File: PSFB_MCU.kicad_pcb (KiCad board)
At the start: 4 copper layers, 238 parts, among them J2 Power_IN, Q1 WMM043N10HGD, Q2 WMM043N10HGD, Q3 WMM043N10HGD, Q4 WMM043N10HGD, U10 USBLC6-2SC6, U11 USBLC6-2SC6, U12 USBLC6-2SC6, U13 USBLC6-2SC6, U14 USBLC6-2SC6, U4 AMS1117-5.0, U5 AMS1117-3.3, U6 LM5176PWP, U7 USBLC6-2SC6, U8 USBLC6-2SC6, U9 USBLC6-2SC6, Y1 16M

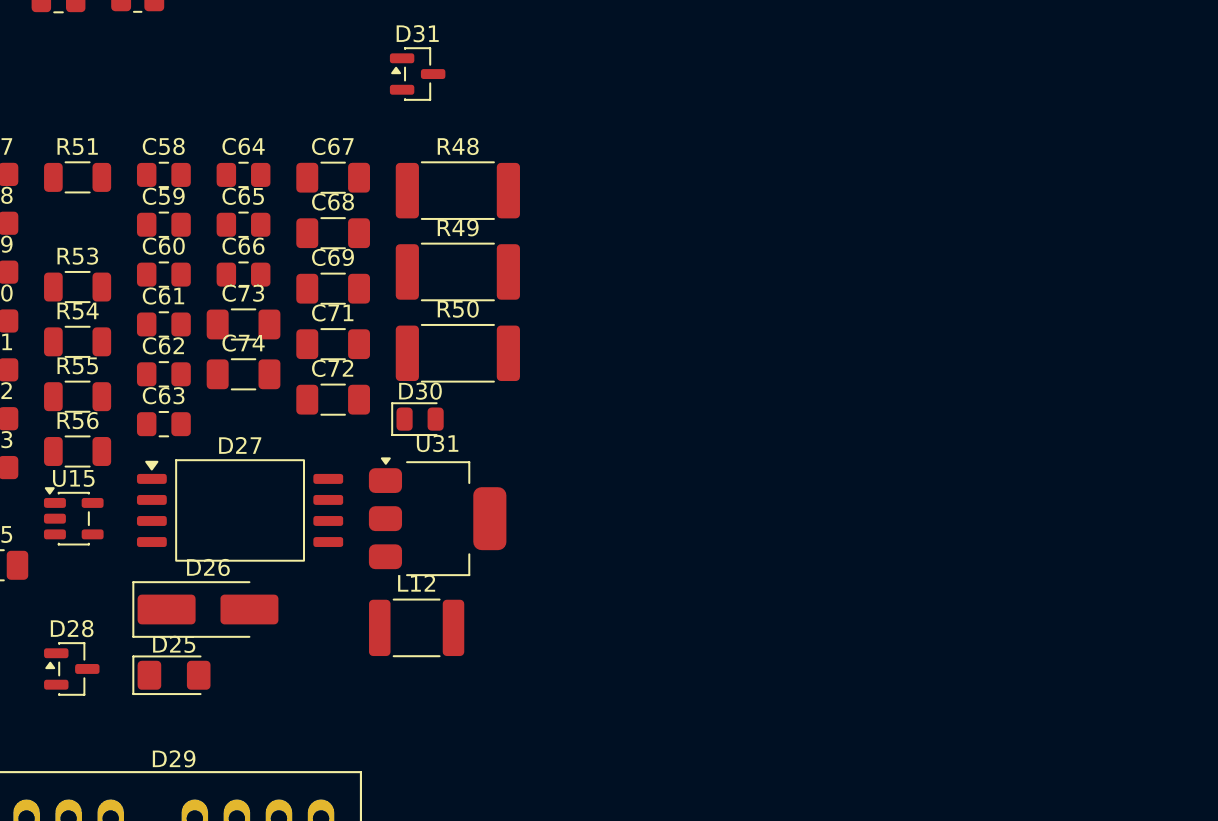
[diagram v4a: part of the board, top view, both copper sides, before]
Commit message: VER1.0: добавил защиту бортового питания для тестов по ISO 7637-2 (Степень III)
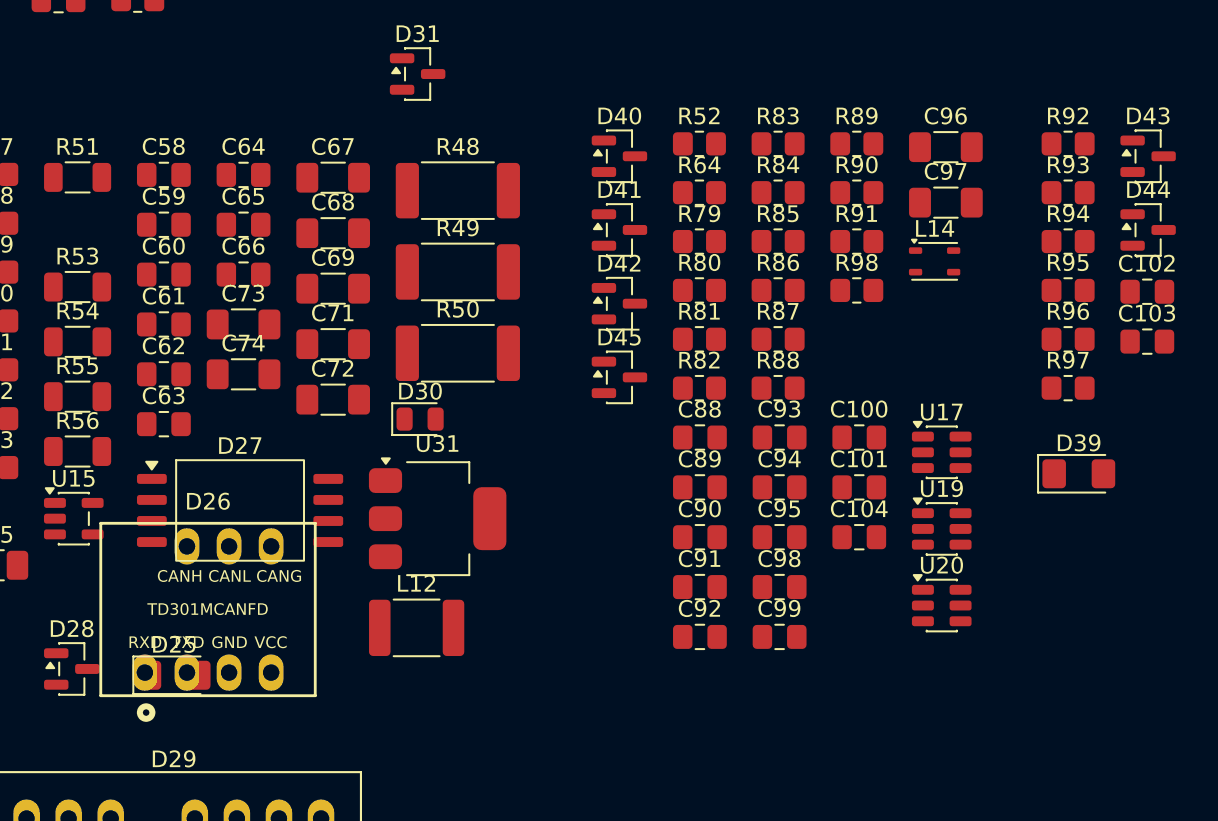
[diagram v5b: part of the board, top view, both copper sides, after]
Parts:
- added C100: 100n, Capacitor_SMD:C_0805_2012Metric_Pad1.18x1.45mm_HandSolder, F.Cu at (229.9, 98.7)
- added C101: 100n, Capacitor_SMD:C_0805_2012Metric_Pad1.18x1.45mm_HandSolder, F.Cu at (229.9, 101.7)
- added C102: 330p, Capacitor_SMD:C_0805_2012Metric_Pad1.18x1.45mm_HandSolder, F.Cu at (247.3, 89.9)
- added C103: 330p, Capacitor_SMD:C_0805_2012Metric_Pad1.18x1.45mm_HandSolder, F.Cu at (247.3, 92.9)
- added C104: 10n, Capacitor_SMD:C_0805_2012Metric_Pad1.18x1.45mm_HandSolder, F.Cu at (229.9, 104.7)
- added C88: 100n, Capacitor_SMD:C_0805_2012Metric_Pad1.18x1.45mm_HandSolder, F.Cu at (220.3, 98.7)
- added C89: 10p, Capacitor_SMD:C_0805_2012Metric_Pad1.18x1.45mm_HandSolder, F.Cu at (220.3, 101.7)
- added C90: 10p, Capacitor_SMD:C_0805_2012Metric_Pad1.18x1.45mm_HandSolder, F.Cu at (220.3, 104.7)
- added C91: 100n, Capacitor_SMD:C_0805_2012Metric_Pad1.18x1.45mm_HandSolder, F.Cu at (220.3, 107.7)
- added C92: 100n, Capacitor_SMD:C_0805_2012Metric_Pad1.18x1.45mm_HandSolder, F.Cu at (220.3, 110.7)
- added C93: 2.2u, Capacitor_SMD:C_0805_2012Metric_Pad1.18x1.45mm_HandSolder, F.Cu at (225.1, 98.7)
- added C94: 2.2u, Capacitor_SMD:C_0805_2012Metric_Pad1.18x1.45mm_HandSolder, F.Cu at (225.1, 101.7)
- added C95: 100n, Capacitor_SMD:C_0805_2012Metric_Pad1.18x1.45mm_HandSolder, F.Cu at (225.1, 104.7)
- added C96: 10u, Capacitor_SMD:C_1206_3216Metric_Pad1.33x1.80mm_HandSolder, F.Cu at (235.2, 81.2)
- added C97: 100n, Capacitor_SMD:C_1206_3216Metric_Pad1.33x1.80mm_HandSolder, F.Cu at (235.2, 84.5)
- added C98: 10p, Capacitor_SMD:C_0805_2012Metric_Pad1.18x1.45mm_HandSolder, F.Cu at (225.1, 107.7)
- added C99: 2.2u, Capacitor_SMD:C_0805_2012Metric_Pad1.18x1.45mm_HandSolder, F.Cu at (225.1, 110.7)
- added D39: ~, LED_SMD:LED_1206_3216Metric_Pad1.42x1.75mm_HandSolder, F.Cu at (243.2, 100.9)
- added D40: ~, Package_TO_SOT_SMD:SOT-23, F.Cu at (215.5, 81.7)
- added D41: ~, Package_TO_SOT_SMD:SOT-23, F.Cu at (215.5, 86.2)
- added D42: ~, Package_TO_SOT_SMD:SOT-23, F.Cu at (215.5, 90.6)
- added D43: ~, Package_TO_SOT_SMD:SOT-23, F.Cu at (247.4, 81.7)
- added D44: ~, Package_TO_SOT_SMD:SOT-23, F.Cu at (247.4, 86.2)
- added D45: ~, Package_TO_SOT_SMD:SOT-23, F.Cu at (215.5, 95.1)
- added L14: ~, Inductor_SMD:L_CommonModeChoke_TDK_ACM2520-2P, F.Cu at (234.5, 88.1)
- added R52: 1k, Resistor_SMD:R_0805_2012Metric_Pad1.20x1.40mm_HandSolder, F.Cu at (220.3, 81.0)
- added R64: 1k, Resistor_SMD:R_0805_2012Metric_Pad1.20x1.40mm_HandSolder, F.Cu at (220.3, 83.9)
- added R79: 0, Resistor_SMD:R_0805_2012Metric_Pad1.20x1.40mm_HandSolder, F.Cu at (220.3, 86.9)
- added R80: 100, Resistor_SMD:R_0805_2012Metric_Pad1.20x1.40mm_HandSolder, F.Cu at (220.3, 89.8)
- added R81: 100, Resistor_SMD:R_0805_2012Metric_Pad1.20x1.40mm_HandSolder, F.Cu at (220.3, 92.8)
- added R82: 0, Resistor_SMD:R_0805_2012Metric_Pad1.20x1.40mm_HandSolder, F.Cu at (220.3, 95.7)
- added R83: 0, Resistor_SMD:R_0805_2012Metric_Pad1.20x1.40mm_HandSolder, F.Cu at (225.0, 81.0)
- added R84: 1k, Resistor_SMD:R_0805_2012Metric_Pad1.20x1.40mm_HandSolder, F.Cu at (225.0, 83.9)
- added R85: 1k, Resistor_SMD:R_0805_2012Metric_Pad1.20x1.40mm_HandSolder, F.Cu at (225.0, 86.9)
- added R86: 59, Resistor_SMD:R_0805_2012Metric_Pad1.20x1.40mm_HandSolder, F.Cu at (225.0, 89.8)
- added R87: 100, Resistor_SMD:R_0805_2012Metric_Pad1.20x1.40mm_HandSolder, F.Cu at (225.0, 92.8)
- added R88: 0, Resistor_SMD:R_0805_2012Metric_Pad1.20x1.40mm_HandSolder, F.Cu at (225.0, 95.7)
- added R89: 0, Resistor_SMD:R_0805_2012Metric_Pad1.20x1.40mm_HandSolder, F.Cu at (229.8, 81.0)
- added R90: 1k, Resistor_SMD:R_0805_2012Metric_Pad1.20x1.40mm_HandSolder, F.Cu at (229.8, 83.9)
- added R91: 1k, Resistor_SMD:R_0805_2012Metric_Pad1.20x1.40mm_HandSolder, F.Cu at (229.8, 86.9)
- added R92: 2k, Resistor_SMD:R_0805_2012Metric_Pad1.20x1.40mm_HandSolder, F.Cu at (242.5, 81.0)
- added R93: 3k, Resistor_SMD:R_0805_2012Metric_Pad1.20x1.40mm_HandSolder, F.Cu at (242.5, 83.9)
- added R94: 120, Resistor_SMD:R_0805_2012Metric_Pad1.20x1.40mm_HandSolder, F.Cu at (242.5, 86.9)
- added R95: 120, Resistor_SMD:R_0805_2012Metric_Pad1.20x1.40mm_HandSolder, F.Cu at (242.5, 89.8)
- added R96: 2k, Resistor_SMD:R_0805_2012Metric_Pad1.20x1.40mm_HandSolder, F.Cu at (242.5, 92.8)
- added R97: 3k, Resistor_SMD:R_0805_2012Metric_Pad1.20x1.40mm_HandSolder, F.Cu at (242.5, 95.7)
- added R98: 59, Resistor_SMD:R_0805_2012Metric_Pad1.20x1.40mm_HandSolder, F.Cu at (229.8, 89.8)
- added U17: TLV3501AIDBV, Package_TO_SOT_SMD:SOT-23-6, F.Cu at (234.9, 99.6)
- added U19: TLV3501AIDBV, Package_TO_SOT_SMD:SOT-23-6, F.Cu at (234.9, 104.2)
- added U20: TLV3501AIDBV, Package_TO_SOT_SMD:SOT-23-6, F.Cu at (234.9, 108.8)
- C10: value 0.1u -> 100n
- D26: value ~ -> TD301MCANFD; footprint Diode_SMD:D_SMA_Handsoldering -> MORNSUN:TD5(3)01MCANFD
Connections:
- net CANH renamed /CANH_1
- net CANL renamed /CANL_1
- net GND_CAN renamed GND_CAN1
- C66 pad 1: /HVoltage_measure_1/HVDC_measure -> /HVDC_MCU
- C87 pad 1: /LVoltage+measure/LVDC_measure -> /LVDC_MCU
- D2 pad 1: CAN1_RXD_MCU -> /CAN1_RXD_MCU
- D2 pad 2: CAN1_TXD_MCU -> /CAN1_TXD_MCU
- D25 pad 1: Net-(D25-K) -> GNDPWR
- D26 pad 1: GNDPWR -> /CAN2_RXD_MCU
- D26 pad 2: Net-(D25-K) -> /CAN2_TXD_MCU
- D28 pad 3: /HVoltage_measure_1/HVDC_measure -> /HVDC_MCU
- D38 pad 3: /LVoltage+measure/LVDC_measure -> /LVDC_MCU
- R62 pad 2: /HVoltage_measure_1/HVDC_measure -> /HVDC_MCU
- R77 pad 2: /LVoltage+measure/LVDC_measure -> /LVDC_MCU
- U1 pad 1: EEPROM_~{CS_MCU} -> /EEPROM_~{CS_MCU}
- U1 pad 2: EEPROM_MISO_MCU -> /EEPROM_MISO_MCU
- U1 pad 5: EEPROM_MOSI_MCU -> /EEPROM_MOSI_MCU
- U1 pad 6: EEPROM_SCK_MCU -> /EEPROM_SCK_MCU
- U3 pad 10: unconnected-(U3-PC2-Pad10) -> /SHDN_OverCurrent_2
- U3 pad 14: unconnected-(U3-PA0-Pad14) -> /HVDC_MCU
- U3 pad 15: unconnected-(U3-PA1-Pad15) -> /LVDC_MCU
- U3 pad 16: unconnected-(U3-PA2-Pad16) -> /Current_measure_1
- U3 pad 17: unconnected-(U3-PA3-Pad17) -> /Current_measure_2
- U3 pad 20: unconnected-(U3-PA4-Pad20) -> /DAC1
- U3 pad 21: /ERROR_LvL1 -> /DAC2
- U3 pad 22: /ERROR_LvL2 -> /BkIN_1
- U3 pad 23: /ERROR_LvL3 -> /TMR8_CH1N
- U3 pad 26: unconnected-(U3-PB0-Pad26) -> /TMR1_CH2N
- U3 pad 33: /GPIO1 -> /BkIN_8
- U3 pad 34: /GPIO2 -> /TMR1_CH1N
- U3 pad 35: /GPIO3 -> /TMR8_CH2N
- U3 pad 36: /GPIO4 -> unconnected-(U3-PB15-Pad36)
- U3 pad 37: /GPIO5 -> /TMR8_CH1
- U3 pad 38: /GPIO6 -> /TMR8_CH2
- U3 pad 39: /GPIO7 -> unconnected-(U3-PC8-Pad39)
- U3 pad 40: /GPIO8 -> unconnected-(U3-PC9-Pad40)
- U3 pad 41: unconnected-(U3-PA8-Pad41) -> /TMR1_CH1
- U3 pad 42: /RS_TXD_MCU -> /TMR1_CH2
- U3 pad 43: /RS_RXD_MCU -> unconnected-(U3-PA10-Pad43)
- U3 pad 44: /CAN_RXD_MCU -> /CAN1_RXD_MCU
- U3 pad 45: /CAN_TXD_MCU -> /CAN1_TXD_MCU
- U3 pad 50: /Solenoid1_MCU -> /EEPROM_~{CS_MCU}
- U3 pad 51: /Solenoid2_MCU -> /EEPROM_SCK_MCU
- U3 pad 52: /Solenoid3_MCU -> /EEPROM_MISO_MCU
- U3 pad 53: /Solenoid4_MCU -> /EEPROM_MOSI_MCU
- U3 pad 57: unconnected-(U3-PB5-Pad57) -> /CAN2_RXD_MCU
- U3 pad 58: unconnected-(U3-PB6-Pad58) -> /CAN2_TXD_MCU
- U3 pad 8: unconnected-(U3-PC0-Pad8) -> /SHDN_OverVoltage
- U3 pad 9: unconnected-(U3-PC1-Pad9) -> /SHDN_OverCurrent_1

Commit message: VER1.0: добавил разъемы для платы вторички
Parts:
- added D46: D_TVS_Small, Diode_SMD:D_SMB, F.Cu at (183.2, 42.1)
- added D47: D_Small, Diode_SMD:D_SMB, F.Cu at (183.2, 47.6)
- added J8: ~, Connector_Molex:Molex_Mini-Fit_Jr_5569-06A2_2x03_P4.20mm_Horizontal, F.Cu at (182.7, 28.9)
- added J9: ~, Connector_Molex:Molex_Mini-Fit_Jr_5569-06A2_2x03_P4.20mm_Horizontal, F.Cu at (198.6, 28.9)
- added R78: 10, Resistor_SMD:R_1206_3216Metric_Pad1.30x1.75mm_HandSolder, F.Cu at (190.4, 41.0)
- D12: footprint Diode_SMD:D_SMB_Handsoldering -> Diode_SMD:D_SMC
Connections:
- C21 pad 2: VIN_filtered -> Net-(D12-A2)
- C22 pad 1: VIN_filtered -> Net-(D12-A2)
- C23 pad 2: VIN_filtered -> Net-(D12-A2)
- D12 pad 2: VIN_filtered -> Net-(D12-A2)
- L2 pad 1: VIN -> Net-(D47-K)
- L2 pad 2: VIN_filtered -> Net-(D12-A2)
- Q1 pad 2: VIN_filtered -> Net-(D12-A2)
